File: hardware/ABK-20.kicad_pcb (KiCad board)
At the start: 2 copper layers, 75 x 80 mm, 73 parts, among them J1 CONN_01X04, J2 CONN_01X04, J4 Con_3-5V, J5 USB_C_6P, J6 Sync_Jumper, SW1 SW_SPST, SW2 SW_Push_LED, SW3 SW_SPDT_MSM, SW4 SW_Push, U1 ATTINY85-20SU, U2 PAM8002, U3 7805

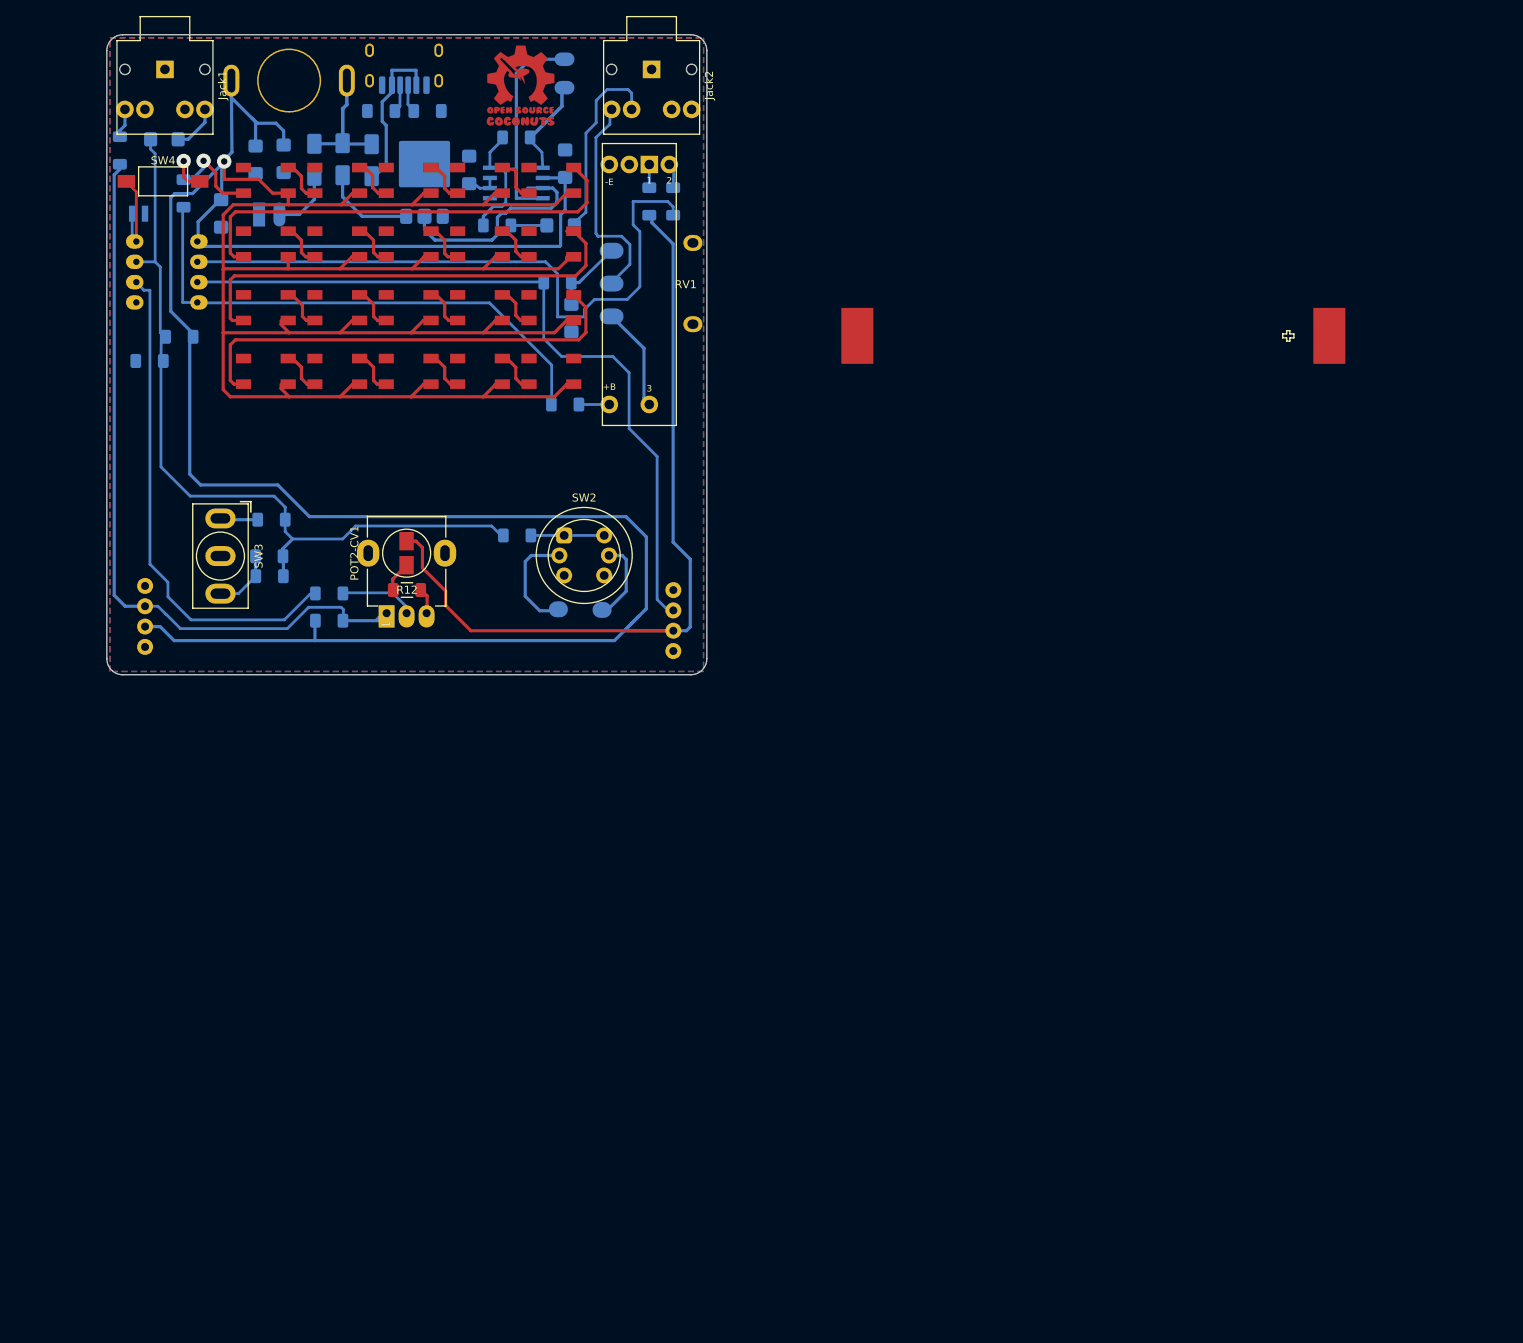
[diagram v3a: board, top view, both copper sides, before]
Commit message: hardware: release Rev 0.2 with flipped backside audio jacks (etched & verified working)
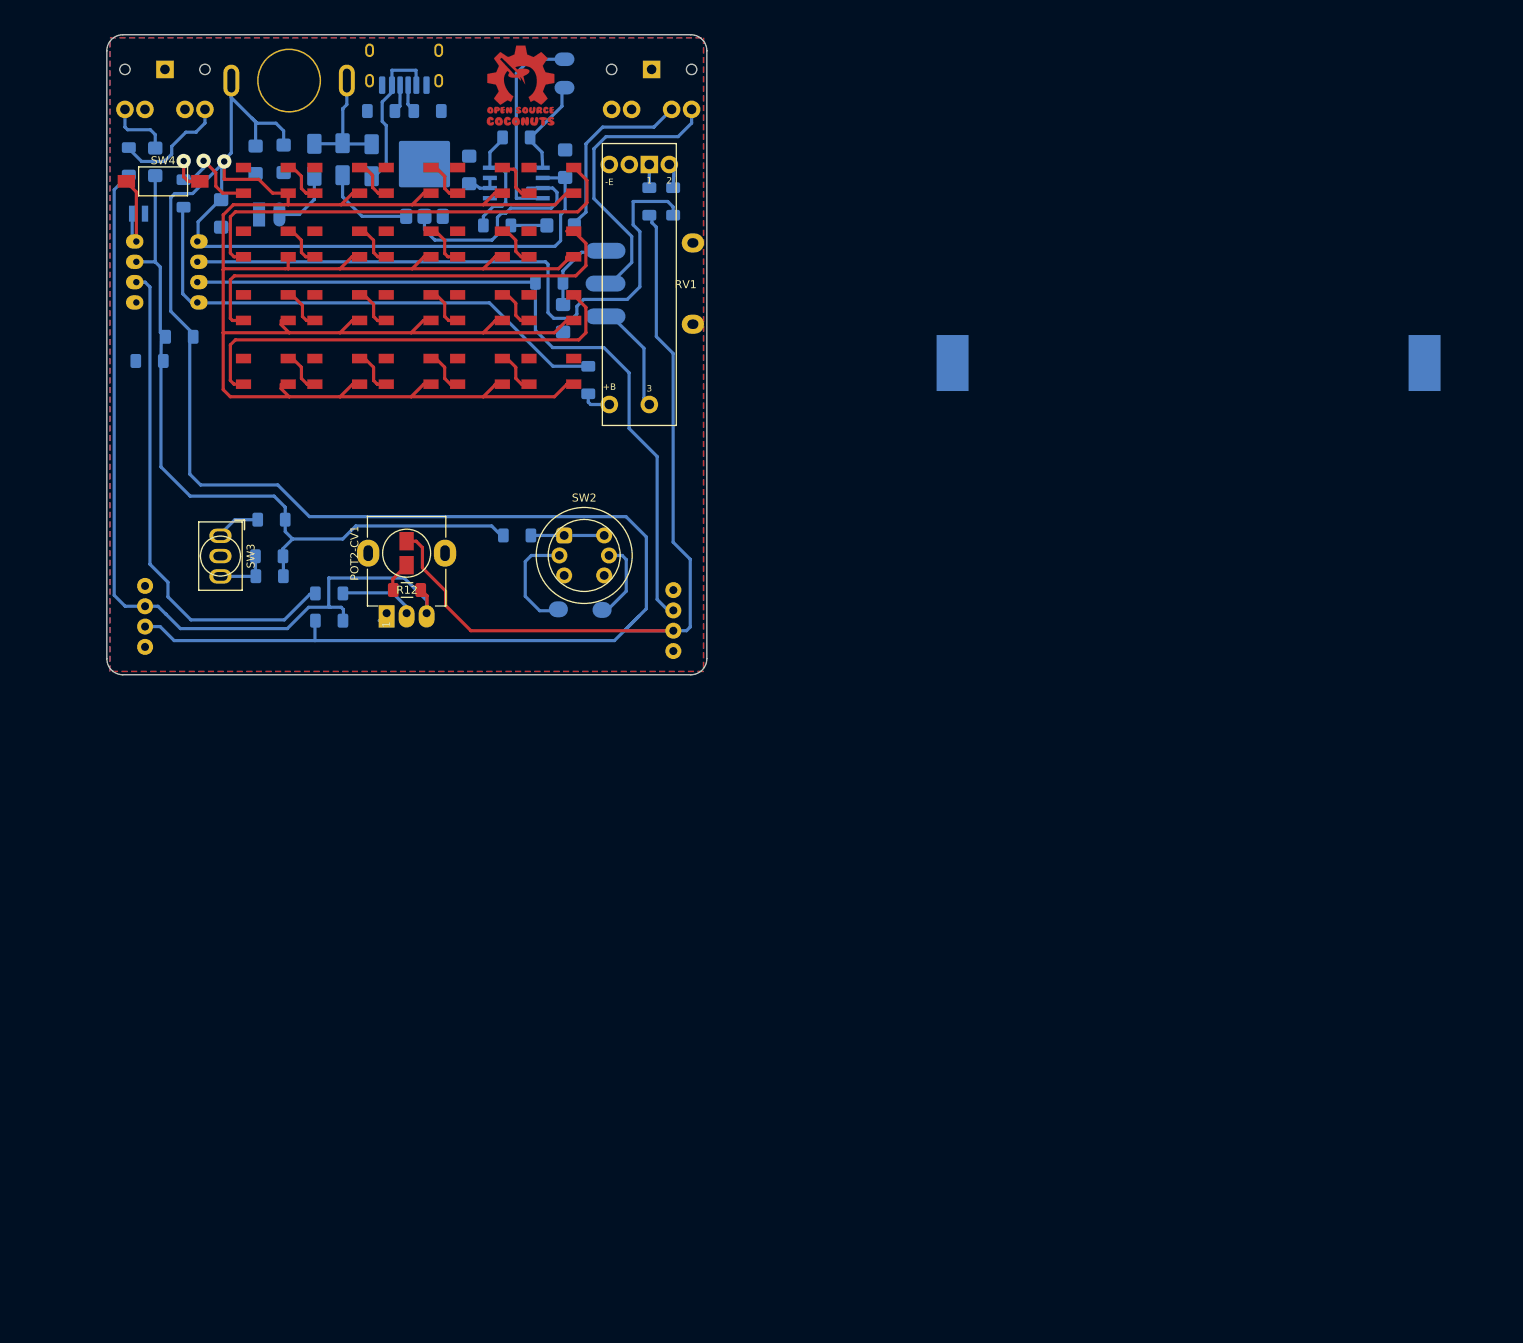
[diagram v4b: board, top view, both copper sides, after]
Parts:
- BT2, Jack1, Jack2: moved to B.Cu
- SW3: footprint 8Bitmixtape_reworked:SW_Toggle_SPDT_MTS-102 -> 8Bitmixtape_reworked:SW_Toggle_SPDT_SubMini_SMTS-103
- moved BT2 12.3 mm to (212.4, 69.6)
- moved R13 4.21 mm to (137.4, 71.8), turned to -90 degrees
- moved C1 3.04 mm to (83.3, 44.6), turned to -90 degrees
- moved R99 1.76 mm to (80.0, 44.5)
- moved C3 1.04 mm to (134.2, 64.1)
- moved R8 1.04 mm to (132.5, 59.7)
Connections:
- POT2-CV1 pad 1: CV_IN -> GND
- POT2-CV1 pad 3: GND -> CV_IN
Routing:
- net Net-(Jack1-T): track 3.68 -> 14.6 mm
- net CV_IN: track 96.0 -> 105.6 mm
- net Net-(Jack2-T): track 27.0 -> 35.1 mm
- net PB3: track 98.4 -> 93.6 mm
- net GND: track 48.7 -> 51.0 mm
- net AudioProg: track 5.86 -> 8.07 mm
- net CV_OUT: track 9.39 -> 10.6 mm
- net But-R: track 8.28 -> 7.18 mm
- net PB0: track 66.2 -> 65.3 mm
- net But-L: track 4.66 -> 5.61 mm
- net PB1: track 95.3 -> 94.6 mm
- net Sound_OUT: track 24.2 -> 23.5 mm
- net PB2/A1: track 80.8 -> 81.4 mm

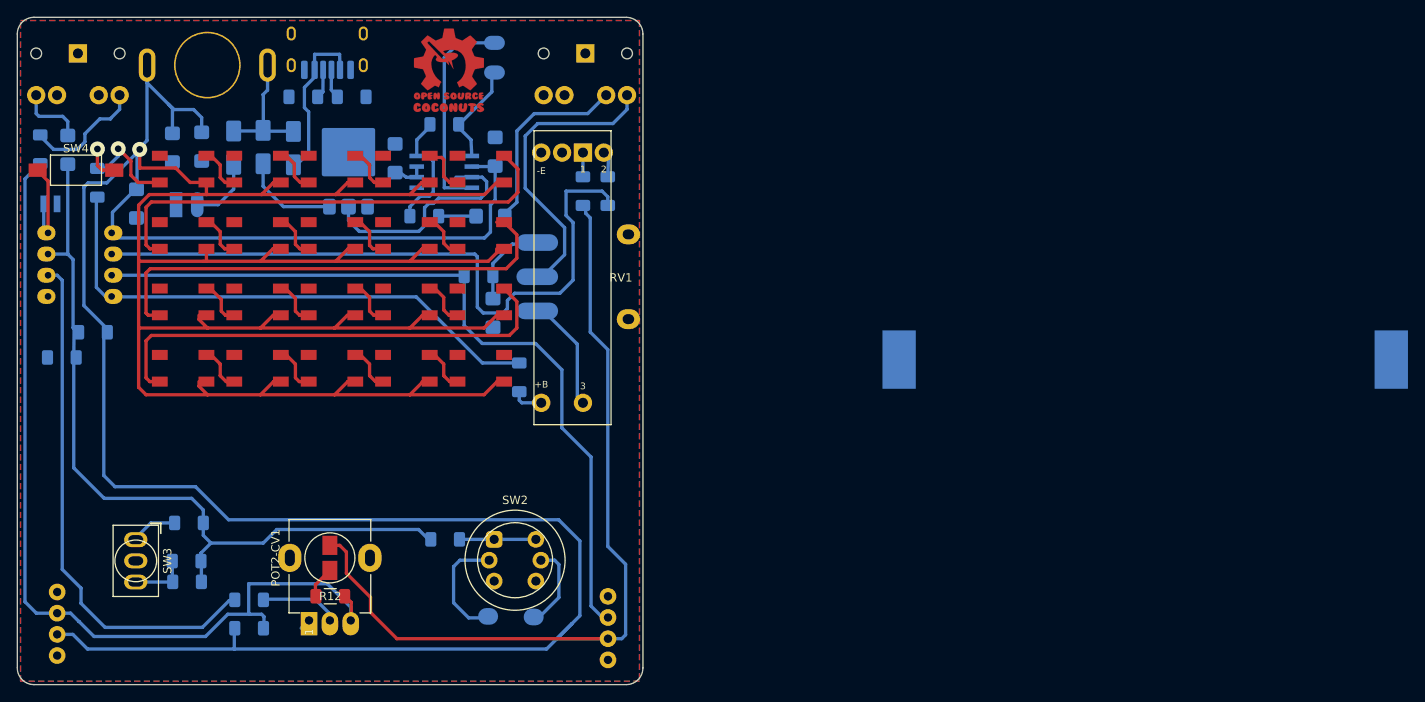
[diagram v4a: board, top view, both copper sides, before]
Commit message: hardware: implement GNDA star grounding, NT1 net tie, and SW2 bi-directional LED circuit for Rev 0.3
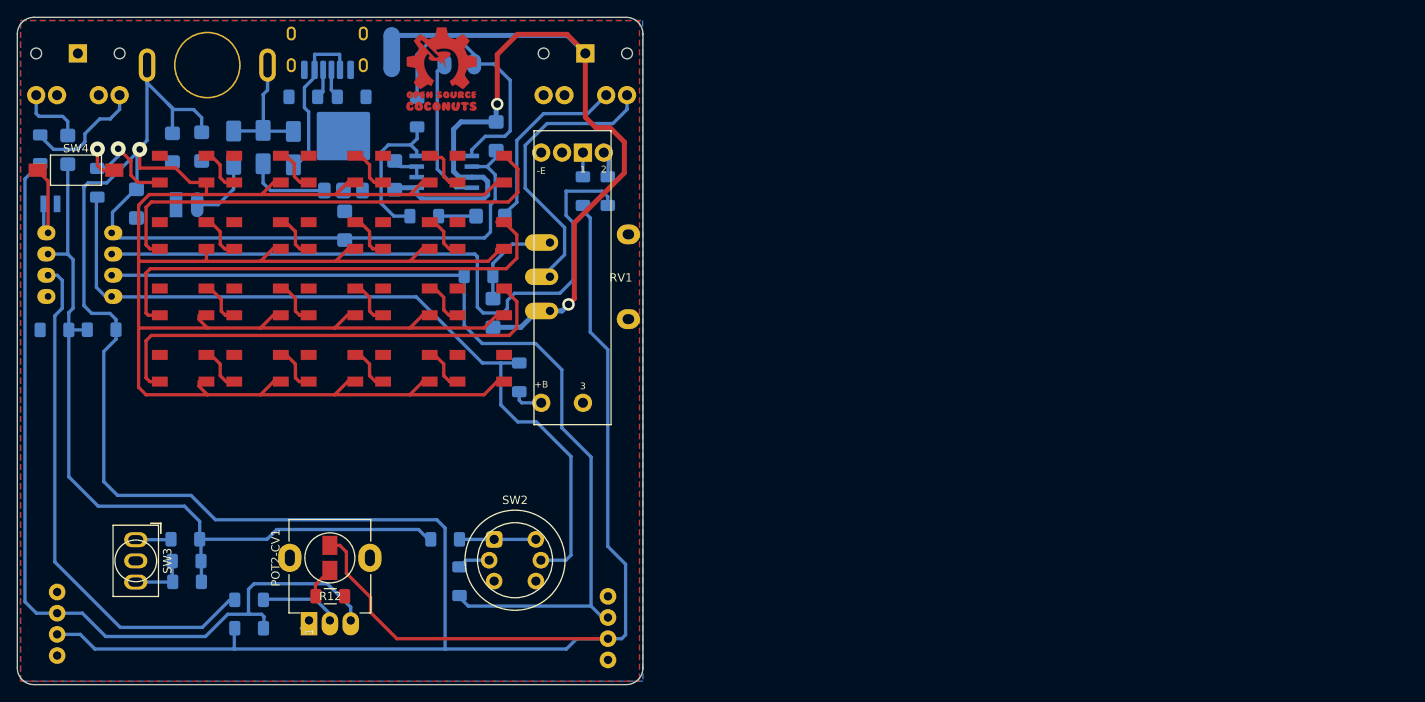
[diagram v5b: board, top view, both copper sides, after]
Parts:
- removed ?: , 
- removed BT2: Battery_Cell, 8Bitmixtape_reworked:BAT_Holder_AAA-new_noHole
- removed Pad4: SP - b, 007_dusjagr:PiezoPad_smd
- added C9: 100nF, 007_dusjagr:C_1210_noGND, B.Cu at (134.6, 42.9)
- added NT1: NetTie_2, NetTie:NetTie-2_SMD_Pad2.0mm, B.Cu at (122.1, 32.8)
- added R19: 1K, 007_dusjagr:R_1206_noGND_sm, B.Cu at (130.2, 96.3)
- moved C7 20.1 mm to (116.5, 53.6)
- moved R15 3.55 mm to (125.1, 40.1), turned to -90 degrees
- moved R2 3.42 mm to (81.7, 66.1)
- moved Speaker1 2.99 mm to (131.5, 34.3), turned to 90 degrees
- moved C6 2.05 mm to (122.5, 47.6), turned to -90 degrees
- moved U3 2.02 mm to (116.3, 44.2)
- moved R3 2.00 mm to (97.4, 91.2)
- moved R1 1.09 mm to (87.3, 66.1)
- moved Ref** 0.88 mm to (127.9, 34.8)
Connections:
- C3 pad 2: GND -> GNDA
- C6 pad 2: GND -> GNDA
- Jack2 pad 1: GND -> GNDA
- POT3-Vol1 pad 3: GND -> GNDA
- SW2 pad A: unconnected-(SW2-PadA) -> Net-(R19-Pad2)
- SW2 pad K: unconnected-(SW2-PadK) -> PB0
- U2 pad 1: GND -> GNDA
- U2 pad 7: GND -> GNDA
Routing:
- net GNDA: track 0.00 -> 119.9 mm, vias 0 -> 2
- net GND: track 51.0 -> 6.92 mm
- net PB0: track 65.3 -> 96.9 mm
- net Net-(U2-OUT-): track 12.4 -> 32.7 mm
- net PB1: track 94.6 -> 111.0 mm
- net unconnected-(SW2-PadA): track 13.6 -> 0.00 mm
- net VCC: track 621.2 -> 607.8 mm
- net unconnected-(SW2-PadK): track 10.3 -> 0.00 mm
- net Net-(U2-OUT+): track 25.7 -> 18.0 mm
- net Net-(R19-Pad2): track 0.00 -> 3.88 mm
- net Net-(U2--IN): track 15.0 -> 18.2 mm
- net PB3: track 93.6 -> 96.3 mm
- net Net-(D1-A): track 11.7 -> 10.0 mm
- net But-L: track 5.61 -> 4.45 mm
- net Sound_OUT: track 23.5 -> 22.8 mm
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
